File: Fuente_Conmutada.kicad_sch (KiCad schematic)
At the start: 54 parts, among them J1 Terminal_220v, J2 Terminal_12v, J3 Vout, Q1 IRF840, Q2 IRF840, T1 Transformer_1P_SS, U1 TL494, U2 IR2110

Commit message: huj
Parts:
- removed D6: B40C2300-1500A, Diode_THT:Diode_Bridge_Vishay_KBPM, symbol Diode_Bridge:B40C2300-1500A
- removed H1, H2, H3, H4: MountingHole_Pad, MountingHole:MountingHole_3.2mm_M3_Pad_Via, symbol Mechanical:MountingHole_Pad
- removed HS1, HS2, HS3: Heatsink, Heatsink:Heatsink_Stonecold_HS-S01_13.21x6.35mm, symbol Mechanical:Heatsink
- added D1: B80C2300-1500B, Diode_THT:Diode_Bridge_Vishay_KBPM, symbol Diode_Bridge:B80C2300-1500B
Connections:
- net GND: now also D1.1 (-)
- net GND_AC: now also D1.4
- net at TH1.1: now also D1.2
- net at C1.1, JP1.1 (A), R1.1: now also D1.3 (+)

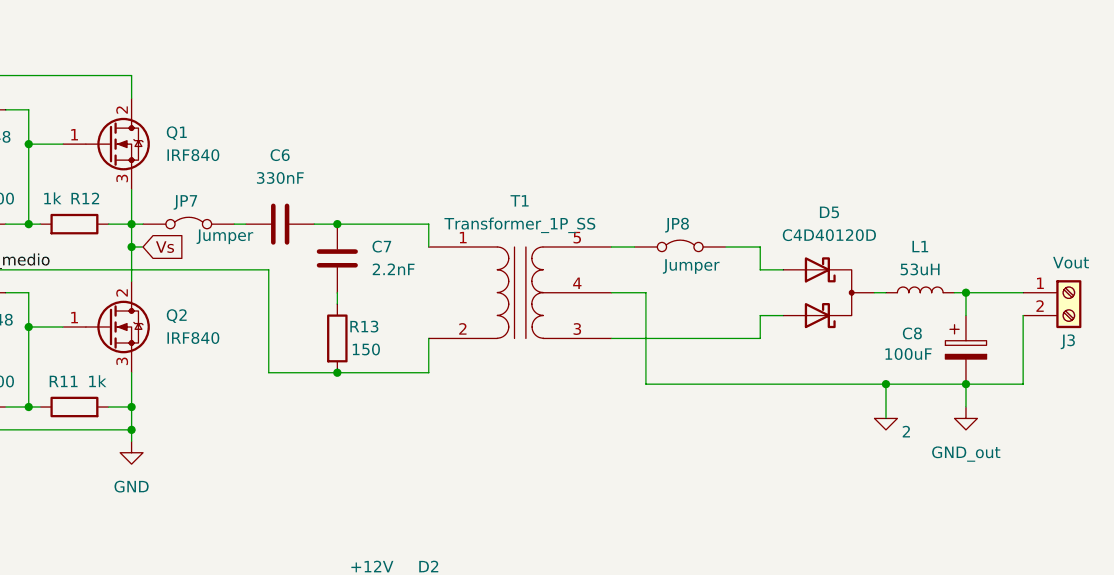
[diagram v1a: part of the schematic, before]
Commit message: Agregado de disipadores
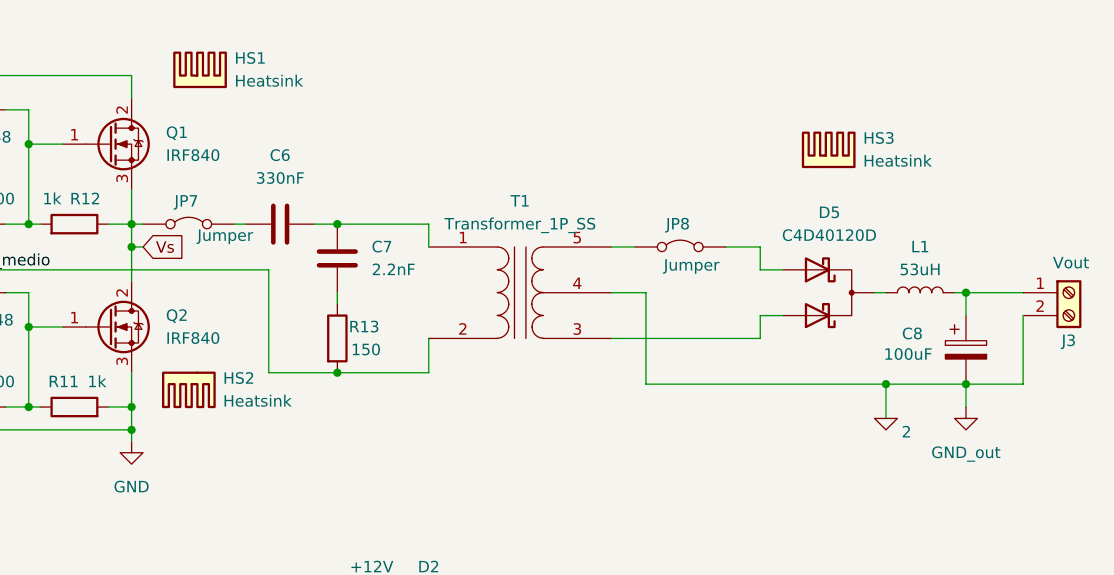
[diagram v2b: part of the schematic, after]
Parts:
- added HS1, HS2, HS3: Heatsink, Heatsink:Heatsink_Stonecold_HS-S02_13.21x9.53mm, symbol Mechanical:Heatsink
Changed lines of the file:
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@@
 	)
 	(symbol
+		(lib_id "Mechanical:Heatsink")
+		(at 170.18 60.96 180)
+		(unit 1)
+		(exclude_from_sim yes)
+		(in_bom yes)
+		(on_board yes)
+		(dnp no)
+		(fields_autoplaced yes)
+		(property "Reference" "HS2"
+			(at 173.99 61.5949 0)
+			(effects
+				(font
+					(size 1.27 1.27)
+				)
+				(justify right)
+			)
+		)
+		(property "Value" "Heatsink"
+			(at 173.99 64.1349 0)
+			(effects
+				(font
+					(size 1.27 1.27)
+				)
+				(justify right)
+			)
+		)
+		(property "Footprint" "Heatsink:Heatsink_Stonecold_HS-S02_13.21x9.53mm"
+			(at 169.8752 60.96 0)
+			(effects
+				(font
+					(size 1.27 1.27)
+				)
+				(hide yes)
+			)
+		)
+		(property "Datasheet" "~"
+			(at 169.8752 60.96 0)
+			(effects
+				(font
+					(size 1.27 1.27)
+				)
+				(hide yes)
+			)
+		)
+		(property "Description" "Heatsink"
+			(at 170.18 60.96 0)
+			(effects
+				(font
+					(size 1.27 1.27)
+				)
+				(hide yes)
+			)
+		)
+		(instances
+			(project "Fuente_Conmutada"
+				(path "/07c86916-f750-4a67-9109-c3040a9c13cc"
+					(reference "HS2")
+					(unit 1)
+				)
+			)
+		)
+	)
+	(symbol
 		(lib_id "Device:R")
 		(at 149.86 110.49 0)
@@
 	)
 	(symbol
+		(lib_id "Mechanical:Heatsink")
+		(at 241.3 38.1 0)
+		(unit 1)
+		(exclude_from_sim yes)
+		(in_bom yes)
+		(on_board yes)
+		(dnp no)
+		(fields_autoplaced yes)
+		(property "Reference" "HS3"
+			(at 245.11 34.9249 0)
+			(effects
+				(font
+					(size 1.27 1.27)
+				)
+				(justify left)
+			)
+		)
+		(property "Value" "Heatsink"
+			(at 245.11 37.4649 0)
+			(effects
+				(font
+					(size 1.27 1.27)
+				)
+				(justify left)
+			)
+		)
+		(property "Footprint" "Heatsink:Heatsink_Stonecold_HS-S02_13.21x9.53mm"
+			(at 241.6048 38.1 0)
+			(effects
+				(font
+					(size 1.27 1.27)
+				)
+				(hide yes)
+			)
+		)
+		(property "Datasheet" "~"
+			(at 241.6048 38.1 0)
+			(effects
+				(font
+					(size 1.27 1.27)
+				)
+				(hide yes)
+			)
+		)
+		(property "Description" "Heatsink"
+			(at 241.3 38.1 0)
+			(effects
+				(font
+					(size 1.27 1.27)
+				)
+				(hide yes)
+			)
+		)
+		(instances
+			(project "Fuente_Conmutada"
+				(path "/07c86916-f750-4a67-9109-c3040a9c13cc"
+					(reference "HS3")
+					(unit 1)
+				)
+			)
+		)
+	)
+	(symbol
 		(lib_id "Transistor_FET:IRF540N")
 		(at 161.29 55.88 0)
@@
 	)
 	(symbol
+		(lib_id "Mechanical:Heatsink")
+		(at 171.45 29.21 0)
+		(unit 1)
+		(exclude_from_sim yes)
+		(in_bom yes)
+		(on_board yes)
+		(dnp no)
+		(fields_autoplaced yes)
+		(property "Reference" "HS1"
+			(at 175.26 26.0349 0)
+			(effects
+				(font
+					(size 1.27 1.27)
+				)
+				(justify left)
+			)
+		)
+		(property "Value" "Heatsink"
+			(at 175.26 28.5749 0)
+			(effects
+				(font
+					(size 1.27 1.27)
+				)
+				(justify left)
+			)
+		)
+		(property "Footprint" "Heatsink:Heatsink_Stonecold_HS-S02_13.21x9.53mm"
+			(at 171.7548 29.21 0)
+			(effects
+				(font
+					(size 1.27 1.27)
+				)
+				(hide yes)
+			)
+		)
+		(property "Datasheet" "~"
+			(at 171.7548 29.21 0)
+			(effects
+				(font
+					(size 1.27 1.27)
+				)
+				(hide yes)
+			)
+		)
+		(property "Description" "Heatsink"
+			(at 171.45 29.21 0)
+			(effects
+				(font
+					(size 1.27 1.27)
+				)
+				(hide yes)
+			)
+		)
+		(instances
+			(project "Fuente_Conmutada"
+				(path "/07c86916-f750-4a67-9109-c3040a9c13cc"
+					(reference "HS1")
+					(unit 1)
+				)
+			)
+		)
+	)
+	(symbol
 		(lib_id "Device:C")
 		(at 116.84 121.92 0)
@@
 		)
 		(instances
-			(project ""
+			(project "Fuente_Conmutada"
 				(path "/07c86916-f750-4a67-9109-c3040a9c13cc"
 					(reference "#PWR017")

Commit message: test
-Le hice test en el esquematico y pcb
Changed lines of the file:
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@@
+	)
+	(junction
+		(at 129.54 81.28)
+		(diameter 0)
+		(color 0 0 0 0)
 	)
 	(junction
@@
 	)
 	(junction
-		(at 129.54 82.55)
-		(diameter 0)
-		(color 0 0 0 0)
-	)
-	(junction
 		(at 163.83 46.99)
 		(diameter 0)
@@
 	(wire
 		(pts
-			(xy 129.54 82.55) (xy 142.24 82.55)
+			(xy 129.54 81.28) (xy 142.24 81.28)
 		)
 		(stroke
@@
 	(wire
 		(pts
-			(xy 142.24 82.55) (xy 142.24 95.25)
+			(xy 142.24 81.28) (xy 142.24 95.25)
 		)
 		(stroke
@@
 	(wire
 		(pts
-			(xy 129.54 78.74) (xy 129.54 82.55)
+			(xy 129.54 78.74) (xy 129.54 81.28)
 		)
 		(stroke
@@
 		)
 		(stroke
+			(width 0)
+			(type default)
+		)
+	)
+	(wire
+		(pts
+			(xy 129.54 81.28) (xy 129.54 82.55)
+		)
+		(stroke

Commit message: Esquemático
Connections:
- net 2: now also D5.3 (A2), T1.3 (SA); no longer T1.4 (SC)
- net Vin/2: now reaches C1.2, C2.1, JP2.1 (A), R1.2, R2.1
- net Vin: now reaches C1.1, D1.3 (+), JP1.1 (A), R1.1
- net V_trafo: now reaches C6.2, JP7.2 (B)
- net Punto_medio: no longer names the net of JP2.2 (B), R13.2, T1.2 (AB)
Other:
- note added: "Conmutador"
- note added: "Driver"
- note added: "PWM"
- note added: "Rectificador"
- note added: "Salida"
- title: (none) -> Fuente Conmutada
- moved on the sheet: C1, C2, C3, C4, C5, C6, C7, C8, D1, D2, D5, F1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

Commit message: {
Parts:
- D2: value BA243 -> 1N4001
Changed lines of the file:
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@@
 		)
 		(property "Value" "TL494"
-			(at 83.566 110.49 0)
+			(at 83.82 111.76 0)
 			(effects
 				(font
@@
 			)
 		)
-		(property "Value" "BA243"
+		(property "Value" "1N4001"
 			(at 167.64 107.95 0)
 			(effects
